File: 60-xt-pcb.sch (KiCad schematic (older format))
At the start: 171 parts, among them J1 Conn_01x04, Q1 2N7002, SW1 SW_Push, U1 MCP1700-3302E_SOT23, U2 STM32F072CBTx

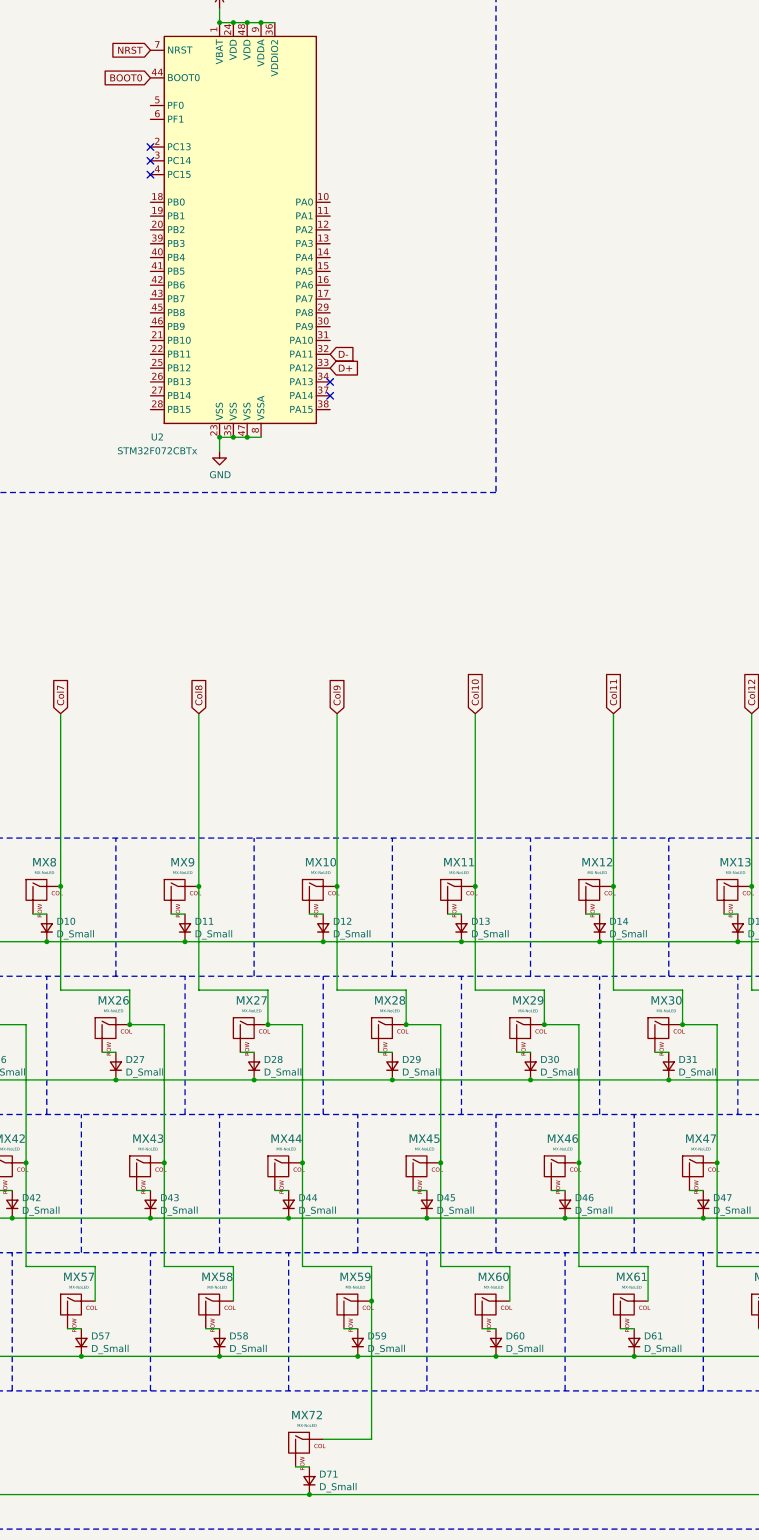
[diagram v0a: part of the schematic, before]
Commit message: finish routing, add logos
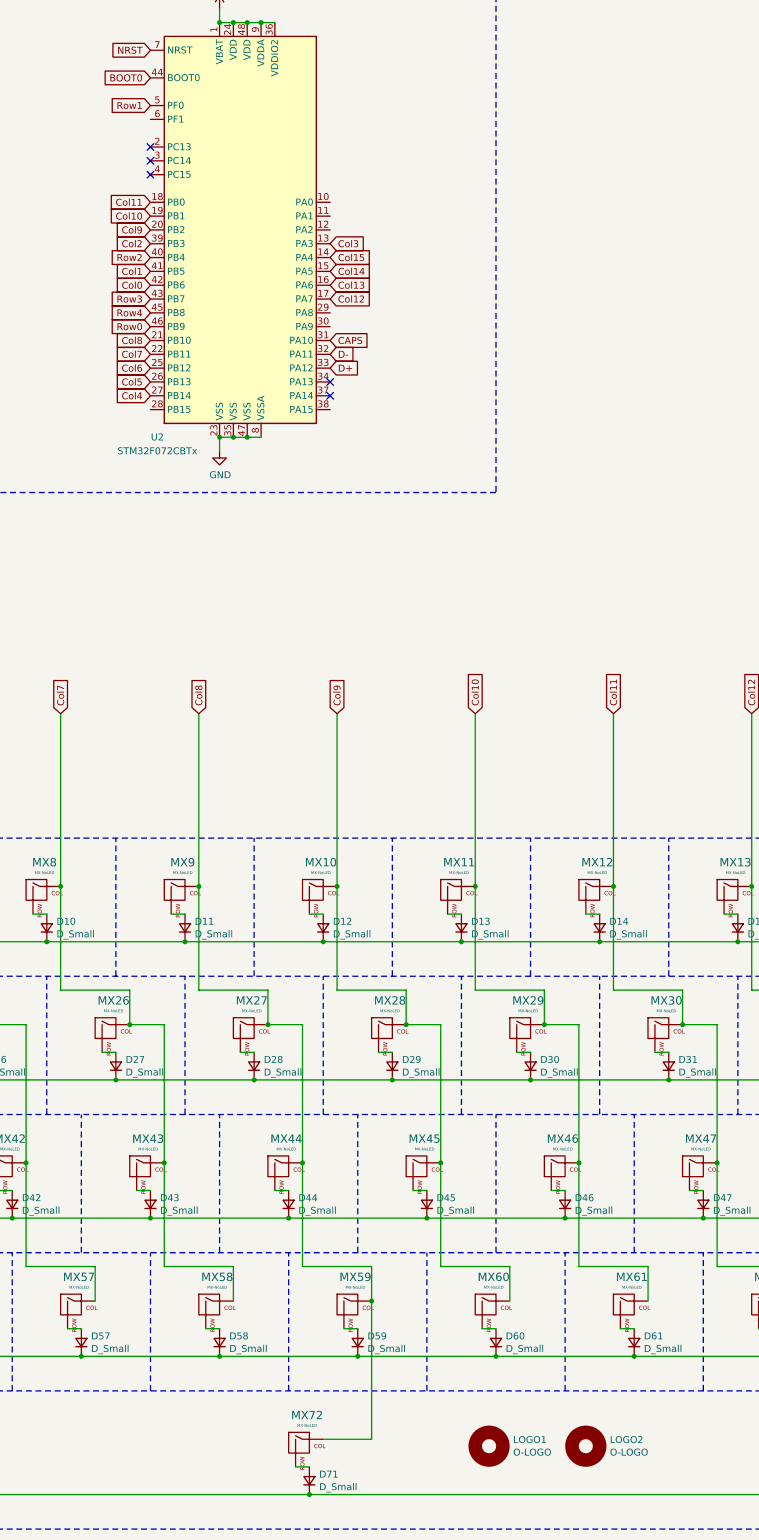
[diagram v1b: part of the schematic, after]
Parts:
- added LOGO1: O-LOGO, board_logos:o-logo-300dpi, symbol logos:O-LOGO
- added LOGO2: O-LOGO, board_logos:o-logo-back-300dpi, symbol logos:O-LOGO
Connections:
- net CAPS: now also U2.31 (PA10)
- net Col0: now also U2.42 (PB6)
- net Col1: now also U2.41 (PB5)
- net Col10: now also U2.19 (PB1)
- net Col11: now also U2.18 (PB0)
- net Col12: now also U2.17 (PA7)
- net Col13: now also U2.16 (PA6)
- net Col14: now also U2.15 (PA5)
- net Col15: now also U2.14 (PA4)
- net Col2: now also U2.39 (PB3)
- net Col3: now also U2.13 (PA3)
- net Col4: now also U2.27 (PB14)
- net Col5: now also U2.26 (PB13)
- net Col6: now also U2.25 (PB12)
- net Col7: now also U2.22 (PB11)
- net Col8: now also U2.21 (PB10)
- net Col9: now also U2.20 (PB2)
- net Row0: now also U2.46 (PB9)
- net Row1: now also U2.5 (PF0)
- net Row2: now also U2.40 (PB4)
- net Row3: now also U2.43 (PB7)
- net Row4: now also U2.45 (PB8)
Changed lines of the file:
@@
 Text GLabel 11100 7600 1    50   Input ~ 0
 Col6
+Text GLabel 13800 4900 2    50   Input ~ 0
+CAPS
+Text GLabel 12500 4800 0    50   Input ~ 0
+Row0
+Text GLabel 12500 4700 0    50   Input ~ 0
+Row4
+Text GLabel 12500 4300 0    50   Input ~ 0
+Row2
+Text GLabel 12500 4600 0    50   Input ~ 0
+Row3
+Text GLabel 12500 4500 0    50   Input ~ 0
+Col0
+Text GLabel 12500 4400 0    50   Input ~ 0
+Col1
+Text GLabel 12500 4200 0    50   Input ~ 0
+Col2
+Text GLabel 13800 4300 2    50   Input ~ 0
+Col15
+Text GLabel 13800 4400 2    50   Input ~ 0
+Col14
+Text GLabel 13800 4500 2    50   Input ~ 0
+Col13
+Text GLabel 13800 4600 2    50   Input ~ 0
+Col12
+Text GLabel 12500 3900 0    50   Input ~ 0
+Col11
+Text GLabel 12500 4000 0    50   Input ~ 0
+Col10
+Text GLabel 12500 4100 0    50   Input ~ 0
+Col9
+Text GLabel 12500 4900 0    50   Input ~ 0
+Col8
+Text GLabel 12500 5000 0    50   Input ~ 0
+Col7
+Text GLabel 12500 5100 0    50   Input ~ 0
+Col6
+Text GLabel 12500 5200 0    50   Input ~ 0
+Col5
+Text GLabel 12500 5300 0    50   Input ~ 0
+Col4
+Text GLabel 13800 4200 2    50   Input ~ 0
+Col3
+Text GLabel 12500 3200 0    50   Input ~ 0
+Row1
+$Comp
+L logos:O-LOGO LOGO1
+U 1 1 600E326D
+P 14950 12900
+F 0 "LOGO1" H 15124 12946 50  0000 L CNN
+F 1 "O-LOGO" H 15124 12855 50  0000 L CNN
+F 2 "board_logos:o-logo-300dpi" H 14950 12900 50  0001 C CNN
+F 3 "" H 14950 12900 50  0001 C CNN
+	1    14950 12900
+	1    0    0    -1
+$EndComp
+$Comp
+L logos:O-LOGO LOGO2
+U 1 1 600E3B17
+P 15650 12900
+F 0 "LOGO2" H 15824 12946 50  0000 L CNN
+F 1 "O-LOGO" H 15824 12855 50  0000 L CNN
+F 2 "board_logos:o-logo-back-300dpi" H 15650 12900 50  0001 C CNN
+F 3 "" H 15650 12900 50  0001 C CNN
+	1    15650 12900
+	1    0    0    -1
+$EndComp
 $EndSCHEMATC
